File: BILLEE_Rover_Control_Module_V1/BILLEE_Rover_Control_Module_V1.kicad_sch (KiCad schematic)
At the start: 0 parts

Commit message: Verified more docs
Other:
- added sheet INPUTS_ESTOP (inputs_estop.kicad_sch)
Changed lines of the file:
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@@
 	(generator_version "10.0")
 	(paper "A4")
+	(title_block
+		(date "2026-07-05")
+		(rev "A")
+	)
+	(sheet
+		(at 17.018 17.526)
+		(size 35.56 16.764)
+		(exclude_from_sim no)
+		(in_bom yes)
+		(on_board yes)
+		(dnp no)
+		(fields_autoplaced yes)
+		(stroke
+			(width 0.1524)
+			(type solid)
+		)
+		(fill
+			(color 0 0 0 0)
+		)
+		(property "Sheetname" "INPUTS_ESTOP"
+			(at 17.018 16.8144 0)
+			(show_name no)
+			(do_not_autoplace no)
+			(effects
+				(font
+					(size 1.27 1.27)
+				)
+				(justify left bottom)
+			)
+		)
+		(property "Sheetfile" "inputs_estop.kicad_sch"
+			(at 17.018 34.8746 0)
+			(show_name no)
+			(do_not_autoplace no)
+			(effects
+				(font
+					(size 1.27 1.27)
+				)
+				(justify left top)
+			)
+		)
+		(instances
+			(project "BILLEE_Rover_Control_Module_V1"
+				(path "/e701dc98-f022-461d-84b5-6b2dd8d89d58"
+					(page "2")
+				)
+			)
+		)
+	)
 	(sheet_instances
 		(path "/"

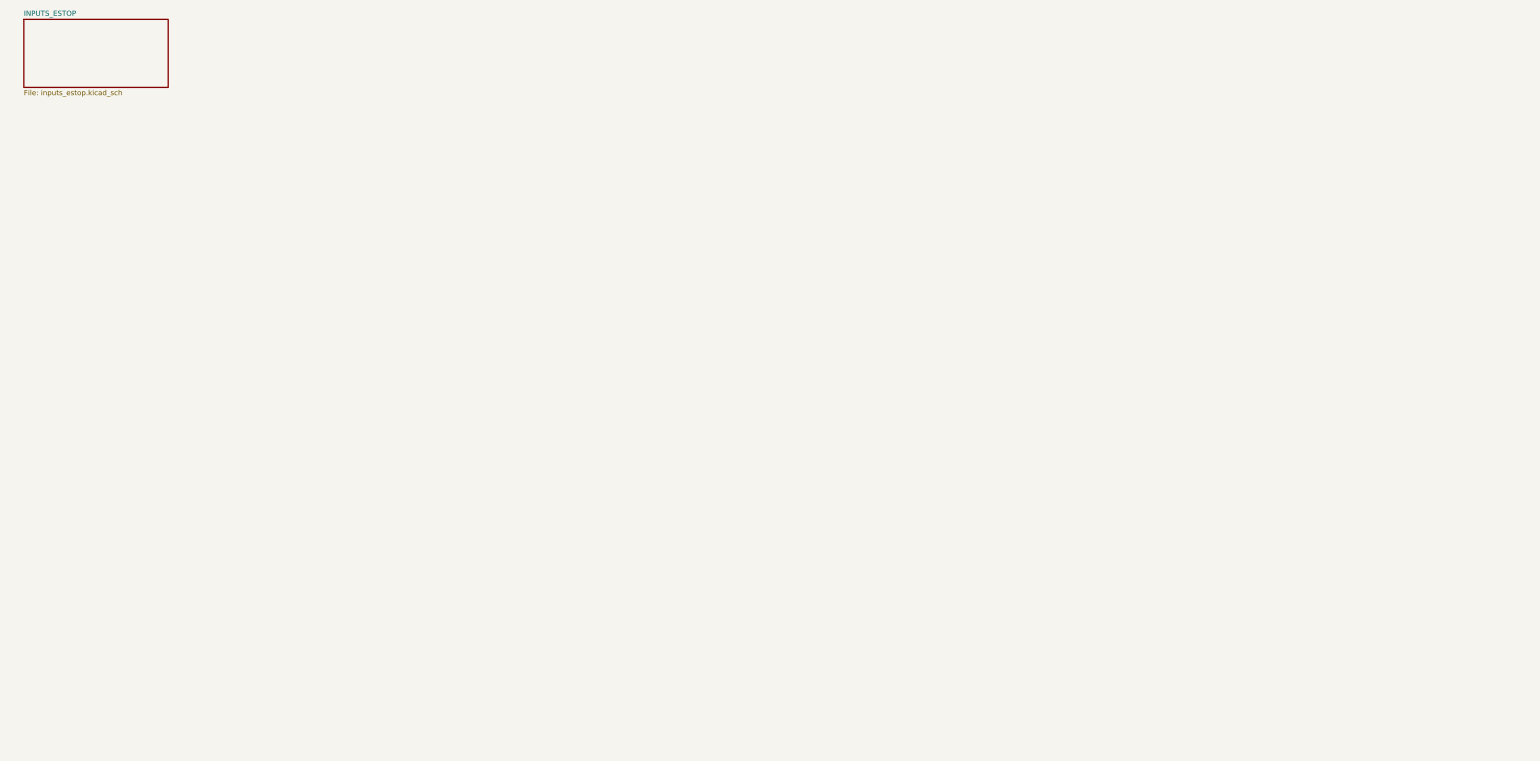
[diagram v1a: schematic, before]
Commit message: Updated Doc with new I2C Device and added ESTOP subsystem to Schematic
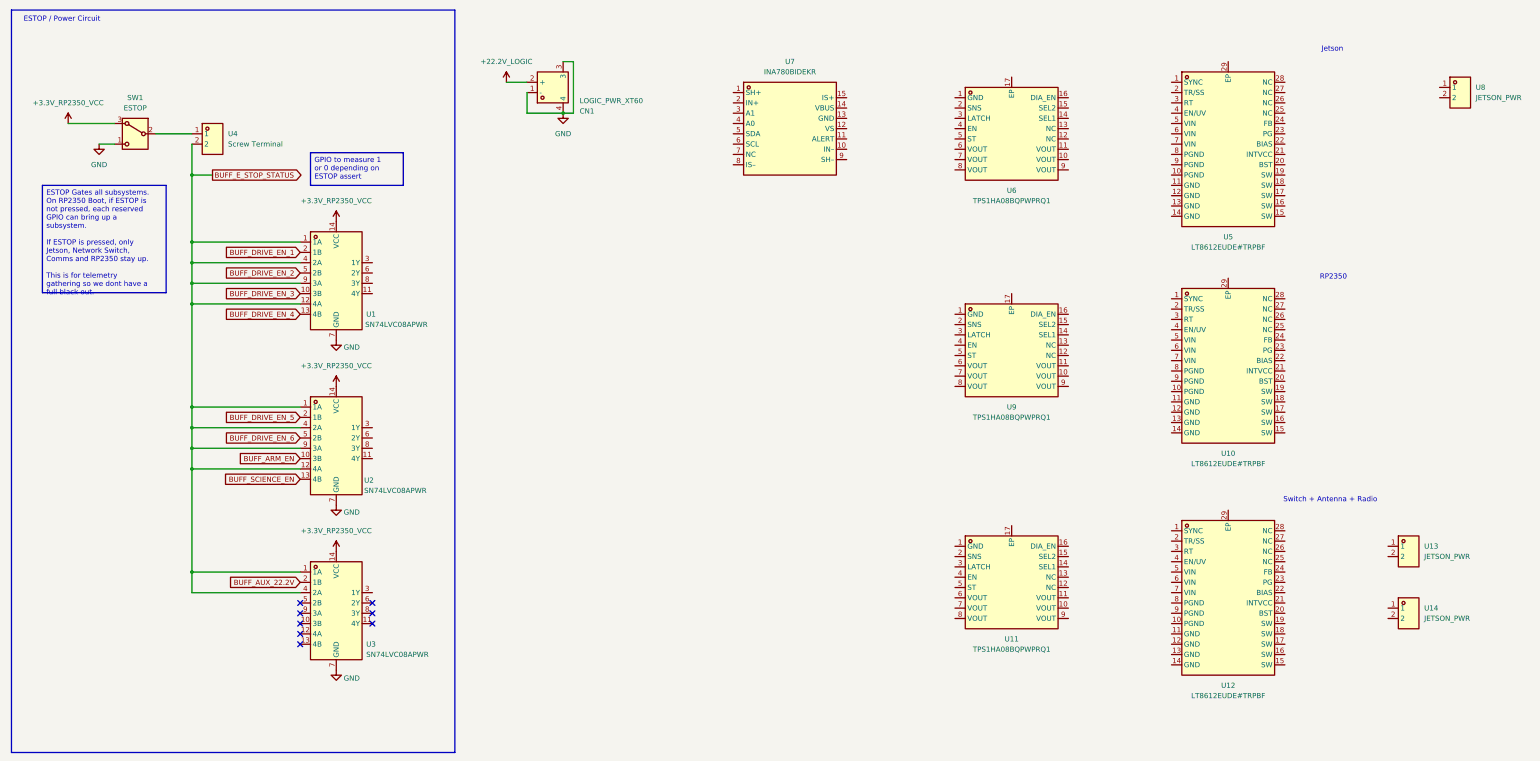
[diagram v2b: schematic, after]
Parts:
- added CN1: LOGIC_PWR_XT60, PDB_LCSC:CONN-TH_XT60PW-M, symbol PDB_LSCS_Libs:XT60PW-M
- added SW1: ESTOP, Button_Switch_SMD:Nidec_Copal_CAS-120A, symbol Switch:SW_Nidec_CAS-120A1
- added U1, U2, U3: SN74LVC08APWR, PDB_LCSC:TSSOP-14_L5.0-W4.4-P0.65-LS6.4-BL, symbol PDB_LSCS_Libs:SN74LVC08APWR
- added U10, U12, U5: LT8612EUDE#TRPBF, PDB_LCSC:QFN-28_L6.0-W3.0-P0.50-BL-EP, symbol PDB_LSCS_Libs:LT8612EUDE#TRPBF
- added U11, U6, U9: TPS1HA08BQPWPRQ1, PDB_LCSC:HTSSOP-16_L5.0-W4.4-P0.65-LS6.4-BL-EP, symbol PDB_LSCS_Libs:TPS1HA08BQPWPRQ1
- added U13, U14, U8: JETSON_PWR, PDB_LCSC:CONN-TH_P5.00_KF301-5.0-2P, symbol PDB_LSCS_Libs:KF301-5.0-2P
- added U4: Screw Terminal, PDB_LCSC:CONN-TH_P5.00_KF301-5.0-2P, symbol PDB_LSCS_Libs:KF301-5.0-2P
- added U7: INA780BIDEKR, PDB_LCSC:VQFN-15_L6.0-W6.0-P0.60-TL, symbol PDB_LSCS_Libs:INA780BIDEKR
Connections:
- new net: SW1.2 (B), U4.1
- new net +22.2V_LOGIC: CN1.2 (+)
- new net +3.3V_RP2350_VCC: SW1.3 (A), U1.14 (VCC), U2.14 (VCC), U3.14 (VCC)
- new net BUFF_ARM_EN: U2.10 (3B)
- new net BUFF_AUX_22.2V: U3.2 (1B)
- new net BUFF_DRIVE_EN_1: U1.2 (1B)
- new net BUFF_DRIVE_EN_2: U1.5 (2B)
- new net BUFF_DRIVE_EN_3: U1.10 (3B)
- new net BUFF_DRIVE_EN_4: U1.13 (4B)
- new net BUFF_DRIVE_EN_5: U2.2 (1B)
- new net BUFF_DRIVE_EN_6: U2.5 (2B)
- new net BUFF_E_STOP_STATUS: U1.1 (1A), U1.12 (4A), U1.4 (2A), U1.9 (3A), U2.1 (1A), U2.12 (4A), U2.4 (2A), U2.9 (3A), U3.1 (1A), U3.4 (2A), U4.2
- new net BUFF_SCIENCE_EN: U2.13 (4B)
- new net GND: CN1.1 (-), CN1.3, CN1.4, SW1.1 (C), U1.7 (GND), U2.7 (GND), U3.7 (GND)
- no-connect marks 0 -> 8
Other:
- removed sheet INPUTS_ESTOP
- note added: "ESTOP / Power Circuit"
- note added: "Jetson"
- note added: "RP2350"
- note added: "Switch + Antenna + Radio"

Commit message: RP 2350A added
Added the RP2350A as a hierarchal sheet and followed the official RP2350A datasheet to do so.
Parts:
- added C1: 0.1uF, symbol Device:C_Small
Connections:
- net +22.2V_LOGIC: now also U7.14 (VBUS), U7.15 (IS+)
- net GND: now also U7.13 (GND)
- net at U7.1 (SH+): now also U7.2 (IN+)
- net at U7.10 (IN–): now also U7.9 (SH–)
- net at U7.12 (VS): now also C1.2
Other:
- added sheet MCU RP2350A (untitled.kicad_sch)
- moved on the sheet: U7

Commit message: Lots of Goodies. Getting the ball rolling
Merged Jasons changed on starting the RP2350.
I refactored his symbols, fixed some connections, and started implementing the buffers as well as all the necessary GPIO connections.
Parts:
- removed C1: 0.1uF, symbol Device:C_Small
- removed CN1: LOGIC_PWR_XT60, PDB_LCSC:CONN-TH_XT60PW-M, symbol PDB_LSCS_Libs:XT60PW-M
- removed SW1: ESTOP, Button_Switch_SMD:Nidec_Copal_CAS-120A, symbol Switch:SW_Nidec_CAS-120A1
- removed U1, U2, U3: SN74LVC08APWR, PDB_LCSC:TSSOP-14_L5.0-W4.4-P0.65-LS6.4-BL, symbol PDB_LSCS_Libs:SN74LVC08APWR
- removed U10, U12, U5: LT8612EUDE#TRPBF, PDB_LCSC:QFN-28_L6.0-W3.0-P0.50-BL-EP, symbol PDB_LSCS_Libs:LT8612EUDE#TRPBF
- removed U11, U6, U9: TPS1HA08BQPWPRQ1, PDB_LCSC:HTSSOP-16_L5.0-W4.4-P0.65-LS6.4-BL-EP, symbol PDB_LSCS_Libs:TPS1HA08BQPWPRQ1
- removed U13, U14, U8: JETSON_PWR, PDB_LCSC:CONN-TH_P5.00_KF301-5.0-2P, symbol PDB_LSCS_Libs:KF301-5.0-2P
- removed U4: Screw Terminal, PDB_LCSC:CONN-TH_P5.00_KF301-5.0-2P, symbol PDB_LSCS_Libs:KF301-5.0-2P
- removed U7: INA780BIDEKR, PDB_LCSC:VQFN-15_L6.0-W6.0-P0.60-TL, symbol PDB_LSCS_Libs:INA780BIDEKR
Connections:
- no-connect marks 8 -> 0
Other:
- added sheet E-STOP Circuit (estop.kicad_sch)
- added sheet Power (power.kicad_sch)
- note removed: "ESTOP / Power Circuit"
- note removed: "Jetson"
- note removed: "RP2350"
- note removed: "Switch + Antenna + Radio"
